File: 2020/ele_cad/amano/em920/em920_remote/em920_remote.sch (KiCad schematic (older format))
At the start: 8 parts, among them SW1 SW_Push, U1 ATtiny85-20PU, U2 TY92SS

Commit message: 緊急停止リモコンのデータ更新
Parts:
- removed U2: TY92SS, em920:TY92SS, symbol em920_remote-rescue:TY92SS-em920
- added U2: TY92SS, em920:TY92SS, symbol em920:TY92SS
- added U3: DCDC_3.3V, em920:DCDC_3.3V, symbol em920:DCDC_3.3V
- BT1: footprint Connector_PinHeader_2.54mm:PinHeader_1x02_P2.54mm_Vertical -> em920:Battery_UM-4_2
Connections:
- wire segments 28 -> 31
- no-connect marks 6 -> 7
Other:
- moved on the sheet: BT1, C1
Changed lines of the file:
@@
 L power:GND #PWR010
 U 1 1 60FEC894
-P 4400 1500
-F 0 "#PWR010" H 4400 1250 50  0001 C CNN
-F 1 "GND" H 4405 1327 50  0000 C CNN
-F 2 "" H 4400 1500 50  0001 C CNN
-F 3 "" H 4400 1500 50  0001 C CNN
-	1    4400 1500
+P 6500 1500
+F 0 "#PWR010" H 6500 1250 50  0001 C CNN
+F 1 "GND" H 6505 1327 50  0000 C CNN
+F 2 "" H 6500 1500 50  0001 C CNN
+F 3 "" H 6500 1500 50  0001 C CNN
+	1    6500 1500
 	1    0    0    -1
 $EndComp
@@
 	1    0    0    -1
 $EndComp
-$Comp
-L em920_remote-rescue:TY92SS-em920 U2
-U 1 1 60FCC105
-P 3500 2700
-F 0 "U2" H 3900 3000 50  0000 C CNN
-F 1 "TY92SS" H 3900 2900 50  0000 C CNN
-F 2 "em920:TY92SS" H 3500 2700 50  0001 C CNN
-F 3 "" H 3500 2700 50  0001 C CNN
-F 4 "em920:TY92SS" H 3500 2700 50  0001 C CNN "Footprint"
-F 5 "TY92SS" H 3500 2700 50  0001 C CNN "Value"
-	1    3500 2700
-	1    0    0    -1
-$EndComp
 NoConn ~ 2400 1400
 $Comp
 L Device:Battery_Cell BT1
 U 1 1 60FEA297
-P 4400 1200
-F 0 "BT1" H 4518 1296 50  0000 L CNN
-F 1 "Battery_Cell" H 4518 1205 50  0000 L CNN
-F 2 "Connector_PinHeader_2.54mm:PinHeader_1x02_P2.54mm_Vertical" V 4400 1260 50  0001 C CNN
-F 3 "~" V 4400 1260 50  0001 C CNN
-	1    4400 1200
+P 6500 1200
+F 0 "BT1" H 6618 1296 50  0000 L CNN
+F 1 "Battery_Cell" H 6618 1205 50  0000 L CNN
+F 2 "em920:Battery_UM-4_2" V 6500 1260 50  0001 C CNN
+F 3 "~" V 6500 1260 50  0001 C CNN
+	1    6500 1200
 	1    0    0    -1
 $EndComp
@@
 L Device:C C1
 U 1 1 60FF4567
-P 5100 1150
-F 0 "C1" H 5250 1200 50  0000 L CNN
-F 1 "0.1uF" H 5250 1150 50  0000 L CNN
-F 2 "Capacitor_THT:C_Disc_D3.0mm_W1.6mm_P2.50mm" H 5138 1000 50  0001 C CNN
-F 3 "~" H 5100 1150 50  0001 C CNN
-F 4 "Capacitor_THT:C_Disc_D3.0mm_W1.6mm_P2.50mm" H 5100 1150 50  0001 C CNN "Footprint"
-F 5 "C1" H 5100 1150 50  0001 C CNN "Value"
-	1    5100 1150
-	1    0    0    -1
-$EndComp
-Connection ~ 4400 1300
-Wire Wire Line
-	4400 1300 4400 1500
-Wire Wire Line
-	4400 1000 5100 1000
-Wire Wire Line
-	4400 1300 5100 1300
-Wire Wire Line
-	4400 900  4400 1000
-Connection ~ 4400 1000
+P 7200 1150
+F 0 "C1" H 7350 1200 50  0000 L CNN
+F 1 "0.1uF" H 7350 1150 50  0000 L CNN
+F 2 "Capacitor_THT:C_Disc_D3.0mm_W1.6mm_P2.50mm" H 7238 1000 50  0001 C CNN
+F 3 "~" H 7200 1150 50  0001 C CNN
+F 4 "Capacitor_THT:C_Disc_D3.0mm_W1.6mm_P2.50mm" H 7200 1150 50  0001 C CNN "Footprint"
+F 5 "C1" H 7200 1150 50  0001 C CNN "Value"
+	1    7200 1150
+	1    0    0    -1
+$EndComp
+Connection ~ 6500 1300
+Wire Wire Line
+	6500 1300 6500 1500
+Wire Wire Line
+	6500 1000 7200 1000
+Wire Wire Line
+	6500 1300 7200 1300
+Wire Wire Line
+	6500 900  6500 1000
+Connection ~ 6500 1000
 $Comp
 L power:+BATT #PWR0101
 U 1 1 60FED62E
-P 4400 900
-F 0 "#PWR0101" H 4400 750 50  0001 C CNN
-F 1 "+BATT" H 4415 1073 50  0000 C CNN
-F 2 "" H 4400 900 50  0001 C CNN
-F 3 "" H 4400 900 50  0001 C CNN
-	1    4400 900
+P 6500 900
+F 0 "#PWR0101" H 6500 750 50  0001 C CNN
+F 1 "+BATT" H 6515 1073 50  0000 C CNN
+F 2 "" H 6500 900 50  0001 C CNN
+F 3 "" H 6500 900 50  0001 C CNN
+	1    6500 900
 	1    0    0    -1
 $EndComp
@@
 Wire Wire Line
 	3000 1300 3200 1300
+$Comp
+L em920:DCDC_3.3V U3
+U 1 1 610177B1
+P 5000 1300
+F 0 "U3" H 5350 1765 50  0000 C CNN
+F 1 "DCDC_3.3V" H 5350 1674 50  0000 C CNN
+F 2 "em920:DCDC_3.3V" H 5300 1650 50  0001 C CNN
+F 3 "" H 5300 1650 50  0001 C CNN
+	1    5000 1300
+	1    0    0    -1
+$EndComp
+$Comp
+L power:GND #PWR011
+U 1 1 61018775
+P 5000 1500
+F 0 "#PWR011" H 5000 1250 50  0001 C CNN
+F 1 "GND" H 5005 1327 50  0000 C CNN
+F 2 "" H 5000 1500 50  0001 C CNN
+F 3 "" H 5000 1500 50  0001 C CNN
+	1    5000 1500
+	1    0    0    -1
+$EndComp
+$Comp
+L power:+3V3 #PWR012
+U 1 1 6101B33D
+P 5700 750
+F 0 "#PWR012" H 5700 600 50  0001 C CNN
+F 1 "+3V3" H 5715 923 50  0000 C CNN
+F 2 "" H 5700 750 50  0001 C CNN
+F 3 "" H 5700 750 50  0001 C CNN
+	1    5700 750
+	1    0    0    -1
+$EndComp
+$Comp
+L power:+BATT #PWR09
+U 1 1 6101B870
+P 5000 750
+F 0 "#PWR09" H 5000 600 50  0001 C CNN
+F 1 "+BATT" H 5015 923 50  0000 C CNN
+F 2 "" H 5000 750 50  0001 C CNN
+F 3 "" H 5000 750 50  0001 C CNN
+	1    5000 750
+	1    0    0    -1
+$EndComp
+NoConn ~ 5700 1250
+Wire Wire Line
+	5700 750  5700 1150
+Wire Wire Line
+	5000 750  5000 1150
+Wire Wire Line
+	5000 1250 5000 1500
+$Comp
+L em920:TY92SS U2
+U 1 1 61021B87
+P 3500 2700
+F 0 "U2" H 3900 2965 50  0000 C CNN
+F 1 "TY92SS" H 3900 2874 50  0000 C CNN
+F 2 "em920:TY92SS" H 3500 2700 50  0001 C CNN
+F 3 "" H 3500 2700 50  0001 C CNN
+	1    3500 2700
+	1    0    0    -1
+$EndComp
 $EndSCHEMATC

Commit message: 緊急停止リモコンの更新
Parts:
- removed U3: DCDC_3.3V, em920:DCDC_3.3V, symbol em920:DCDC_3.3V
- added U3: AE-XCL102D333CR-G, em920:AE-XCL102D333CR-G, symbol em920:AE-XCL102D333CR-G
- BT1: footprint em920:Battery_UM-4_2 -> Battery:BatteryHolder_Keystone_103_1x20mm
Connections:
- wire segments 31 -> 33
- no-connect marks 7 -> 9
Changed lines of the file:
@@
 F 0 "BT1" H 6618 1296 50  0000 L CNN
 F 1 "Battery_Cell" H 6618 1205 50  0000 L CNN
-F 2 "em920:Battery_UM-4_2" V 6500 1260 50  0001 C CNN
+F 2 "Battery:BatteryHolder_Keystone_103_1x20mm" V 6500 1260 50  0001 C CNN
 F 3 "~" V 6500 1260 50  0001 C CNN
 	1    6500 1200
@@
 	3000 1300 3200 1300
 $Comp
-L em920:DCDC_3.3V U3
-U 1 1 610177B1
-P 5000 1300
-F 0 "U3" H 5350 1765 50  0000 C CNN
-F 1 "DCDC_3.3V" H 5350 1674 50  0000 C CNN
-F 2 "em920:DCDC_3.3V" H 5300 1650 50  0001 C CNN
-F 3 "" H 5300 1650 50  0001 C CNN
-	1    5000 1300
-	1    0    0    -1
-$EndComp
-$Comp
 L power:GND #PWR011
 U 1 1 61018775
-P 5000 1500
-F 0 "#PWR011" H 5000 1250 50  0001 C CNN
-F 1 "GND" H 5005 1327 50  0000 C CNN
-F 2 "" H 5000 1500 50  0001 C CNN
-F 3 "" H 5000 1500 50  0001 C CNN
-	1    5000 1500
+P 4850 1500
+F 0 "#PWR011" H 4850 1250 50  0001 C CNN
+F 1 "GND" H 4855 1327 50  0000 C CNN
+F 2 "" H 4850 1500 50  0001 C CNN
+F 3 "" H 4850 1500 50  0001 C CNN
+	1    4850 1500
 	1    0    0    -1
 $EndComp
@@
 L power:+3V3 #PWR012
 U 1 1 6101B33D
-P 5700 750
-F 0 "#PWR012" H 5700 600 50  0001 C CNN
-F 1 "+3V3" H 5715 923 50  0000 C CNN
-F 2 "" H 5700 750 50  0001 C CNN
-F 3 "" H 5700 750 50  0001 C CNN
-	1    5700 750
+P 4750 900
+F 0 "#PWR012" H 4750 750 50  0001 C CNN
+F 1 "+3V3" H 4765 1073 50  0000 C CNN
+F 2 "" H 4750 900 50  0001 C CNN
+F 3 "" H 4750 900 50  0001 C CNN
+	1    4750 900
 	1    0    0    -1
 $EndComp
-$Comp
-L power:+BATT #PWR09
-U 1 1 6101B870
-P 5000 750
-F 0 "#PWR09" H 5000 600 50  0001 C CNN
-F 1 "+BATT" H 5015 923 50  0000 C CNN
-F 2 "" H 5000 750 50  0001 C CNN
-F 3 "" H 5000 750 50  0001 C CNN
-	1    5000 750
-	1    0    0    -1
-$EndComp
-NoConn ~ 5700 1250
-Wire Wire Line
-	5700 750  5700 1150
-Wire Wire Line
-	5000 750  5000 1150
-Wire Wire Line
-	5000 1250 5000 1500
 $Comp
 L em920:TY92SS U2
@@
 	1    0    0    -1
 $EndComp
+$Comp
+L em920:AE-XCL102D333CR-G U3
+U 1 1 6105883F
+P 5650 1100
+F 0 "U3" H 5975 885 50  0000 C CNN
+F 1 "AE-XCL102D333CR-G" H 5975 976 50  0000 C CNN
+F 2 "em920:AE-XCL102D333CR-G" H 5950 1400 50  0001 C CNN
+F 3 "" H 5950 1400 50  0001 C CNN
+	1    5650 1100
+	-1   0    0    1
+$EndComp
+Wire Wire Line
+	5000 900  5000 1100
+$Comp
+L power:+BATT #PWR09
+U 1 1 6101B870
+P 5000 900
+F 0 "#PWR09" H 5000 750 50  0001 C CNN
+F 1 "+BATT" H 5015 1073 50  0000 C CNN
+F 2 "" H 5000 900 50  0001 C CNN
+F 3 "" H 5000 900 50  0001 C CNN
+	1    5000 900
+	1    0    0    -1
+$EndComp
+Wire Wire Line
+	5000 1200 4850 1200
+Wire Wire Line
+	4850 1200 4850 1500
+Wire Wire Line
+	5000 1300 4750 1300
+Wire Wire Line
+	4750 1300 4750 900
+NoConn ~ 5650 1100
+NoConn ~ 5650 1200
+NoConn ~ 5650 1300
 $EndSCHEMATC

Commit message: 回路データの更新
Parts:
- added R3: R, Resistor_THT:R_Axial_DIN0207_L6.3mm_D2.5mm_P2.54mm_Vertical, symbol Device:R
- added SW2: SW_SPST, em920:SlideSW, symbol Switch:SW_SPST
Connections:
- net labels added: IN, PWR_SW
- wire segments 33 -> 47
- no-connect marks 9 -> 6
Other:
- moved on the sheet: BT1, C1, U2

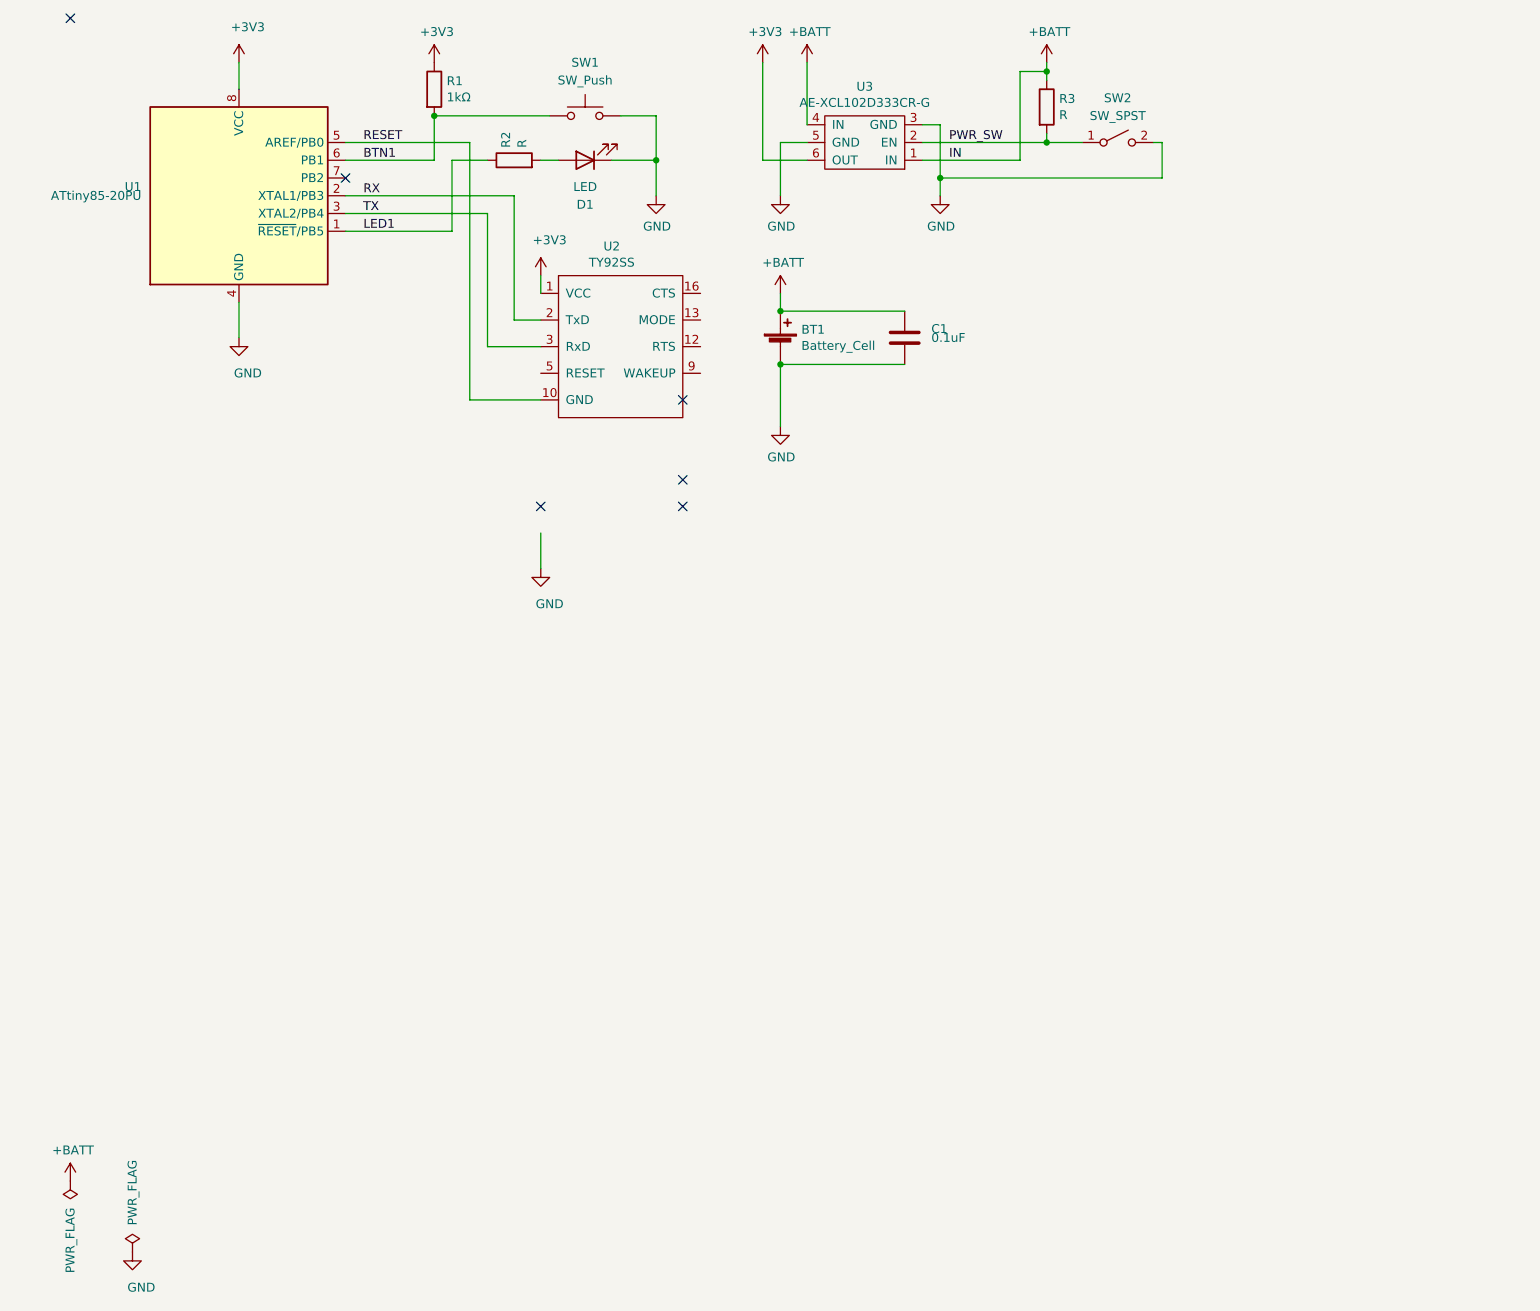
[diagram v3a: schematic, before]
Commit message: 緊急停止リモコンの回路更新
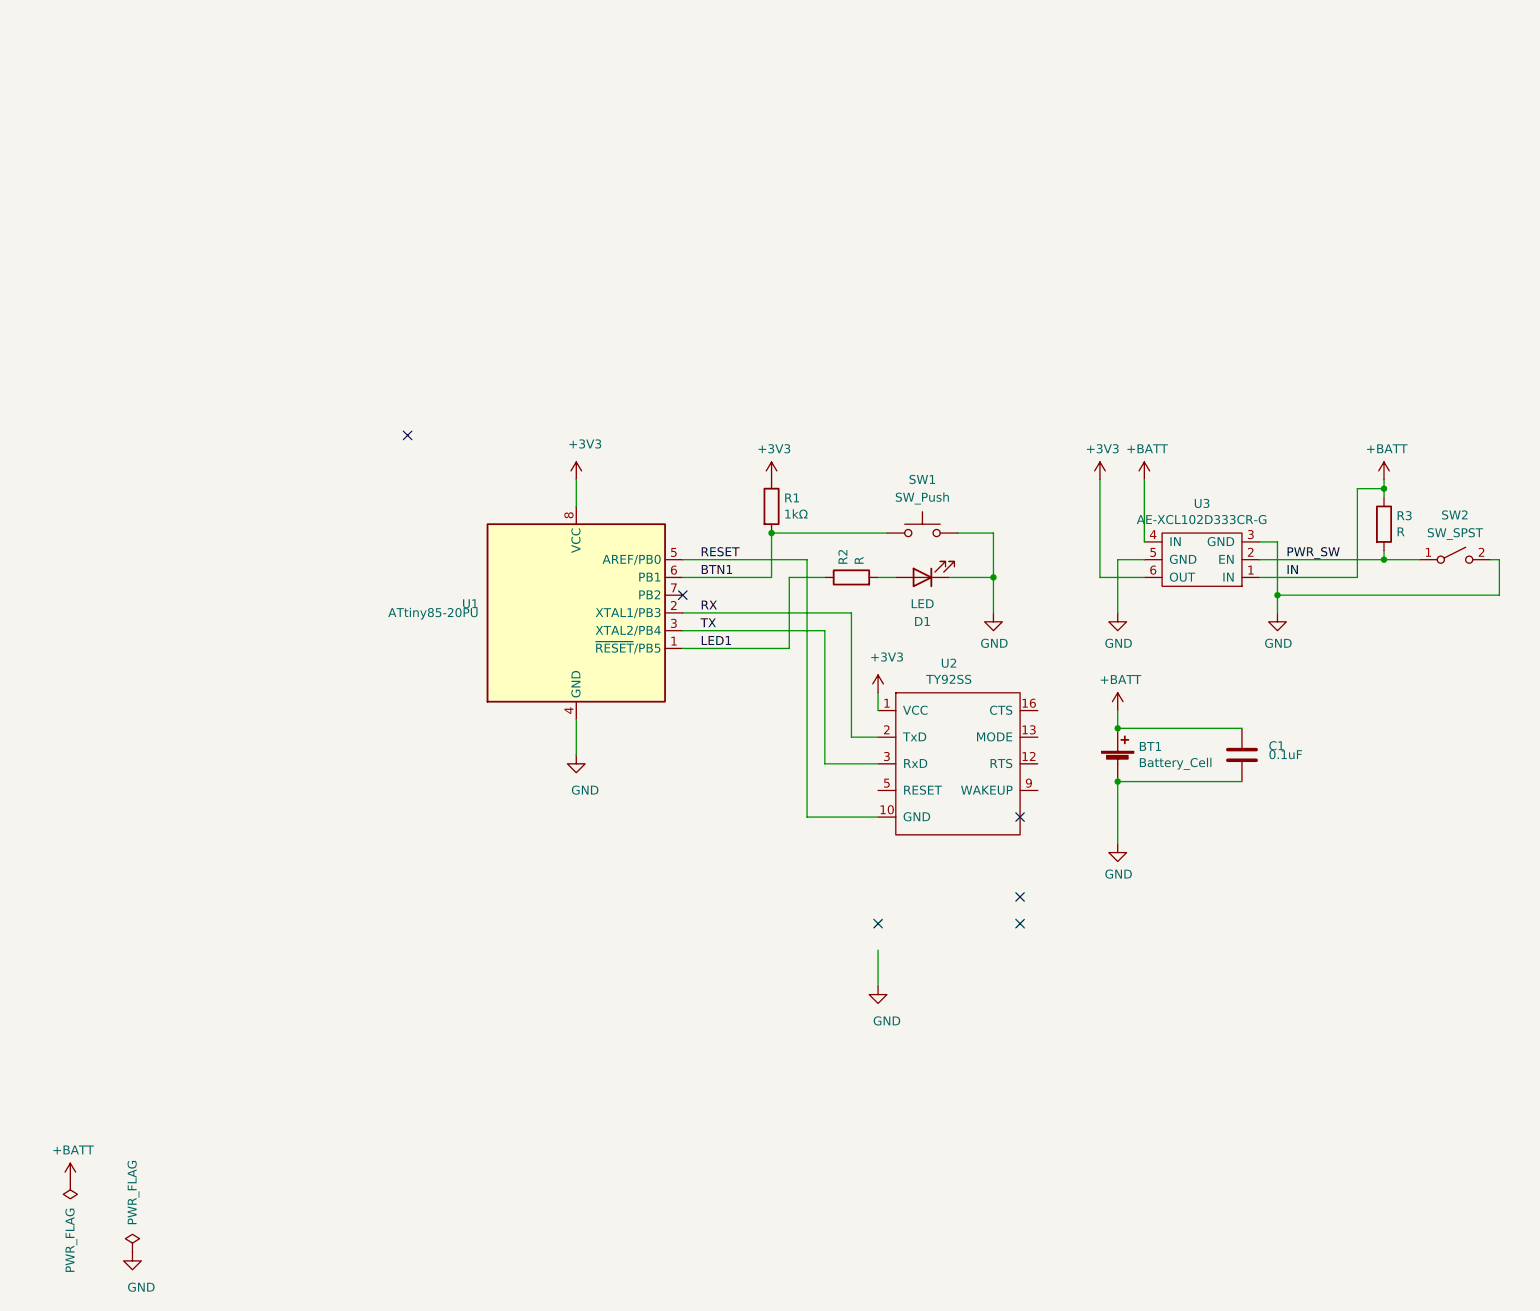
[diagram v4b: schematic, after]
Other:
- moved on the sheet: BT1, C1, D1, R1, R2, R3, SW1, SW2, U1, U2, U3
